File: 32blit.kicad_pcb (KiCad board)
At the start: 4 copper layers, 150 x 65 mm, 121 parts, among them CN1 LIPO BATTERY, J1 1X02PICOBLADE, J3 1X02JST_SH, Q5 DMN3023L, U1 SN74AHC1G02, U11 BQ24295, U22 MT25QL256ABA1EW7-0SIT, U3 AP3031KTR-G1 - ref 200mV, U5 PAM8301, U6 AP2112, U8 74VHC4053AFT, X1 MicroSD

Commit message: Try to fix button footprints
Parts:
- ABXY0: value ABXY -> Val**
- D2: value NSR0530HT1G -> (none)
- DPAD0: value DPAD -> Val**

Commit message: Update PCB from schematic
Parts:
- ABXY0: value Val** -> ABXY
- D1: value NSR0530HT1G -> DIODE-SCHOTTKY
- D2: value (none) -> NSR0530HT1G
- DPAD0: value Val** -> DPAD
- JOYSTICK0: value FLIP_TYPE_0.5_5P -> FPC-05WAY0.5
- L1: value NRS5030T1R0NMGJ -> NRS5030
- SJ1: value (none) -> SOLDERJUMPER
- STM32H750: value (none) -> STM32H750VB
- U$3: value FCI 10118193-0001LF -> USBMICROB
- U22: value MT25QL256ABA1EW7-0SIT -> SPI_QUAD_FLASH
- U4: value (none) -> ACCEL_LIS3DHTR
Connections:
- net 48_VCAP renamed /MCU/48_VCAP
- net 73_VCAP renamed /MCU/73_VCAP
- net BOOT0 renamed /MCU/BOOT0
- net EXTENSION_GPIO renamed /MCU/EXTENSION_GPIO
- net LEDA renamed /LCDs and Power/LEDA
- net LEDK renamed /LCDs and Power/LEDK
- net OUT+ renamed /Peripherals/OUT+
- net OUT- renamed /Peripherals/OUT-
- net REGN renamed Net-(U11-REGN)
- net SWCLK renamed /MCU/SWCLK
- net SWDIO renamed /MCU/SWDIO
- net USB_DFU_DM renamed /MCU/USB_DFU_DM
- net USB_DFU_DP renamed /MCU/USB_DFU_DP
- net USB_MAIN_DM renamed /MCU/USB_MAIN_DM
- net USB_MAIN_DP renamed /MCU/USB_MAIN_DP
- net USB_SWAP renamed /MCU/USB_SWAP
- net USER_LEFT1 renamed /MCU/USER_LEFT1
- net USER_LEFT2 renamed /MCU/USER_LEFT2
- net USER_RIGHT1 renamed /MCU/USER_RIGHT1
- net USER_RIGHT2 renamed /MCU/USER_RIGHT2
- net XTAL_IN renamed /MCU/XTAL_IN
- net XTAL_OUT renamed /MCU/XTAL_OUT
- net ~{RESET} renamed /MCU/~{RESET}
- STM32H750 pad 3: (no net) -> unconnected-(STM32H750-03_PE4/SPI4_NSS-Pad3)
- STM32H750 pad 93: (no net) -> unconnected-(STM32H750-93_PB7/I2C2_SDA-Pad93)
- U$19 pad 2: (no net) -> Net-(U$19-GND-Pad2)
- U$19 pad 4: (no net) -> Net-(U$19-GND-Pad2)
- U11 pad 4: (no net) -> unconnected-(U11-STAT-Pad4)
- U11 pad 7: (no net) -> unconnected-(U11-INT-Pad7)
- U4 pad 2: (no net) -> unconnected-(U4-NC@1-Pad2)
- U4 pad 3: (no net) -> unconnected-(U4-NC@2-Pad3)
- U4 pad 9: (no net) -> unconnected-(U4-INT2-Pad9)
- U8 pad 3: (no net) -> unconnected-(U8-1Z-Pad3)
- X1 pad 1: (no net) -> unconnected-(X1-DAT2-Pad1)
- X1 pad 8: (no net) -> unconnected-(X1-DAT1-Pad8)
- X1 pad CD1: (no net) -> unconnected-(X1-CARD_DETECT-PadCD1)

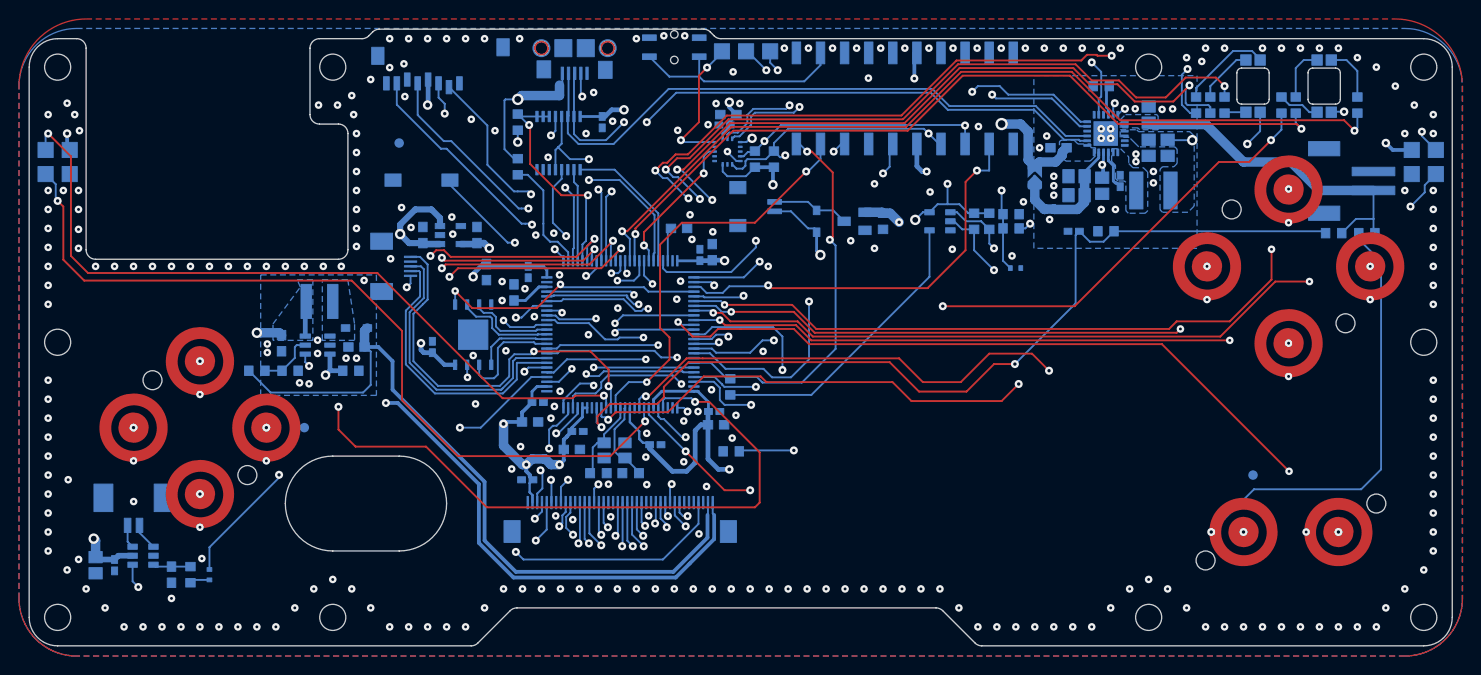
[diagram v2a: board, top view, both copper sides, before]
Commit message: Use kicad footprints for resistors/capacitors
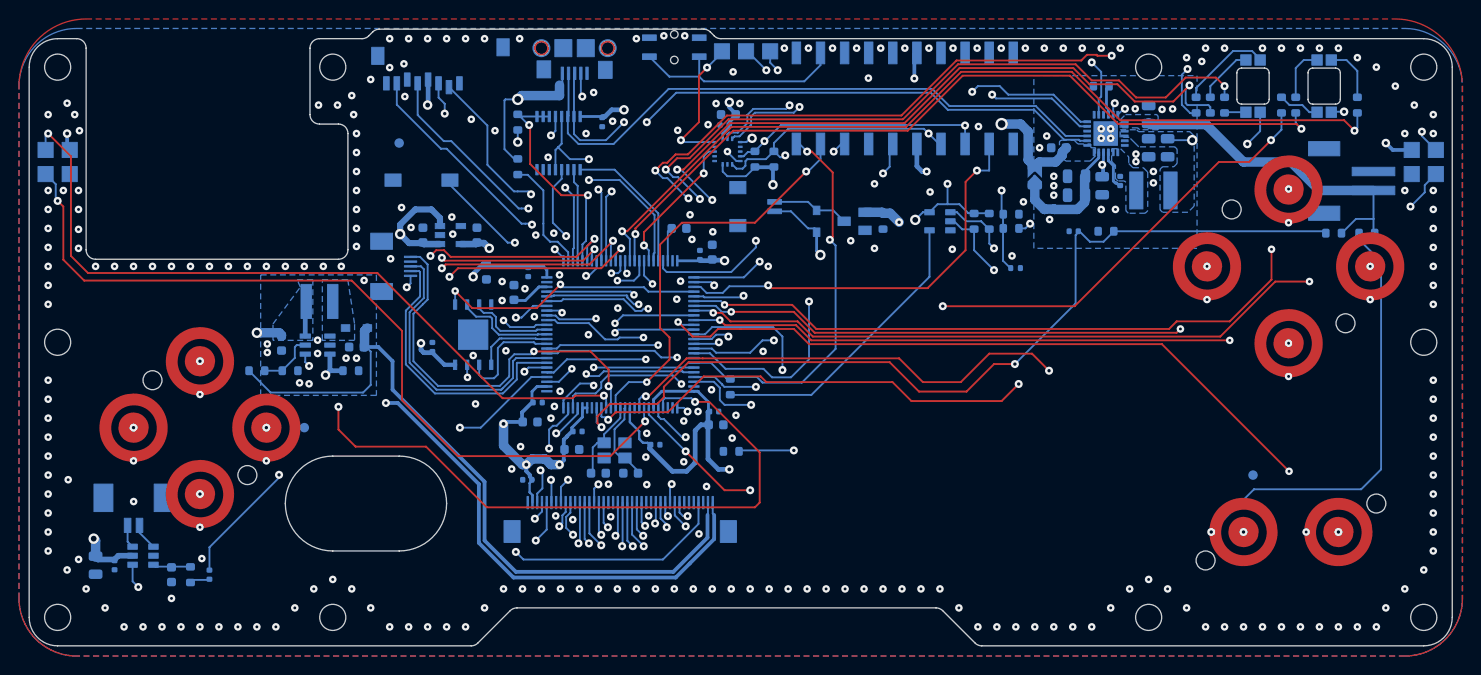
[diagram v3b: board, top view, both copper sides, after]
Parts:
- BAT_THERM0: footprint 32blit:0402@1 -> Resistor_SMD:R_0402_1005Metric
- C1, C17, C2, C22, C26, C27, C28, C29, C3, C30, C32, C33, C34, C39: footprint 32blit:C0603 -> Capacitor_SMD:C_0603_1608Metric
- C10, C11, C14, C20, C21, C25, C4, C40, C5, C6, C7, C8, C9: footprint 32blit:C0402K -> Capacitor_SMD:C_0402_1005Metric
- C12, C36, C37, C41, C42, C43, C44: footprint 32blit:C0805 -> Capacitor_SMD:C_0805_2012Metric
- C23: footprint 32blit:0402 -> Capacitor_SMD:C_0402_1005Metric
- C24, C35: footprint 32blit:C0603K -> Capacitor_SMD:C_0603_1608Metric
- R1, R10, R11, R12, R13, R17, R18, R19, R2, R20, R21, R24, R26, R29, R3, R36, R37, R38, R39, R40, R5, R6, R7, R8, R9: footprint 32blit:R0603 -> Resistor_SMD:R_0603_1608Metric

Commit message: More footprint replacements
This involved some adjusting for pad sizes
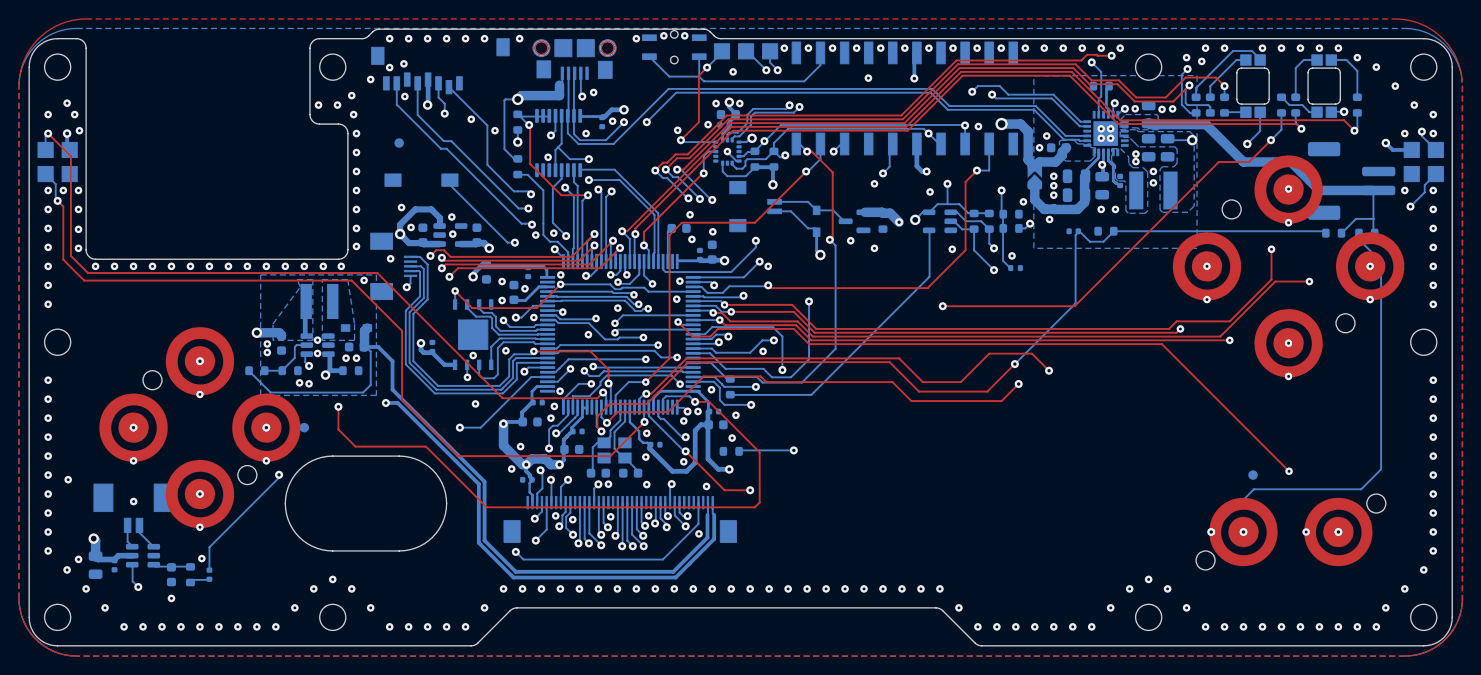
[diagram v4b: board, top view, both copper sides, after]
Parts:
- CN1: footprint 32blit:JST-PH-2-SMT-RA -> Connector_JST:JST_PH_S2B-PH-SM4-TB_1x02-1MP_P2.00mm_Horizontal
- D1: value DIODE-SCHOTTKY -> NSR0530HT1G
- L1: footprint 32blit:NRS5030 -> Inductor_SMD:L_Taiyo-Yuden_NR-50xx
- L2: footprint 32blit:NR4018 -> Inductor_SMD:L_Taiyo-Yuden_NR-40xx
- Q5: footprint 32blit:SOT23 -> Package_TO_SOT_SMD:SOT-23
- STM32H750: footprint 32blit:LQFP-100 -> Package_QFP:LQFP-100_14x14mm_P0.5mm
- U$17, U$22, U$23: footprint 32blit:FIDUCIAL-1MM -> Fiducial:Fiducial_1mm_Mask2mm
- U$19: footprint 32blit:TSX-3225 -> Crystal:Crystal_SMD_SeikoEpson_TSX3225-4Pin_3.2x2.5mm
- U1, U6: footprint 32blit:SOT-23-5 -> Package_TO_SOT_SMD:SOT-23-5
- U22: value SPI_QUAD_FLASH -> MT25QL256ABA1EW7-0SIT
- U3: footprint 32blit:SOT23-6L -> Package_TO_SOT_SMD:SOT-23-6
- U4: footprint 32blit:LGA16_3X3MM -> Package_LGA:LGA-16_3x3mm_P0.5mm_LayoutBorder3x5y
- U5: footprint 32blit:SOT-23-6 -> Package_TO_SOT_SMD:SOT-23-6
- U8: footprint 32blit:TSSOP-16-TI -> Package_SO:TSSOP-16_4.4x5mm_P0.65mm
- moved CN1 1.40 mm to (212.9, 88.5), turned to 90 degrees
- turned Q5 to 180 degrees
- turned STM32H750 to 90 degrees
- turned U1 to 180 degrees
- turned U3 to 180 degrees
- turned U5 to 180 degrees
- turned U6 to 0 degrees
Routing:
- net /MCU/~{RESET}: track 66.5 -> 65.7 mm
- net LCD_B7: track 34.2 -> 35.1 mm
- net DPAD_UP: track 63.7 -> 64.4 mm
- net DPAD_LEFT: track 67.1 -> 67.7 mm
